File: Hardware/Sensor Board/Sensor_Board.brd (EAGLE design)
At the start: 100 x 80 mm, 3 parts

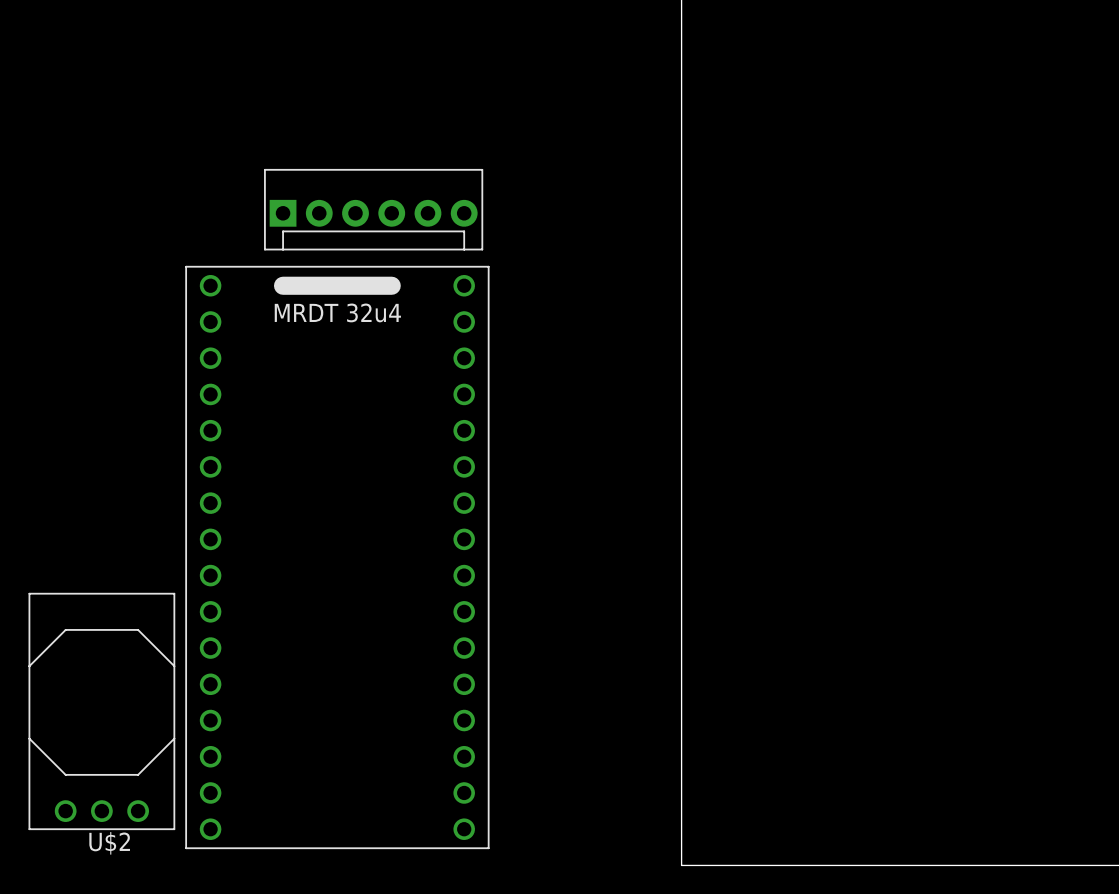
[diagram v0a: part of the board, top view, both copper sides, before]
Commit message: Added most of the components onto the Science board
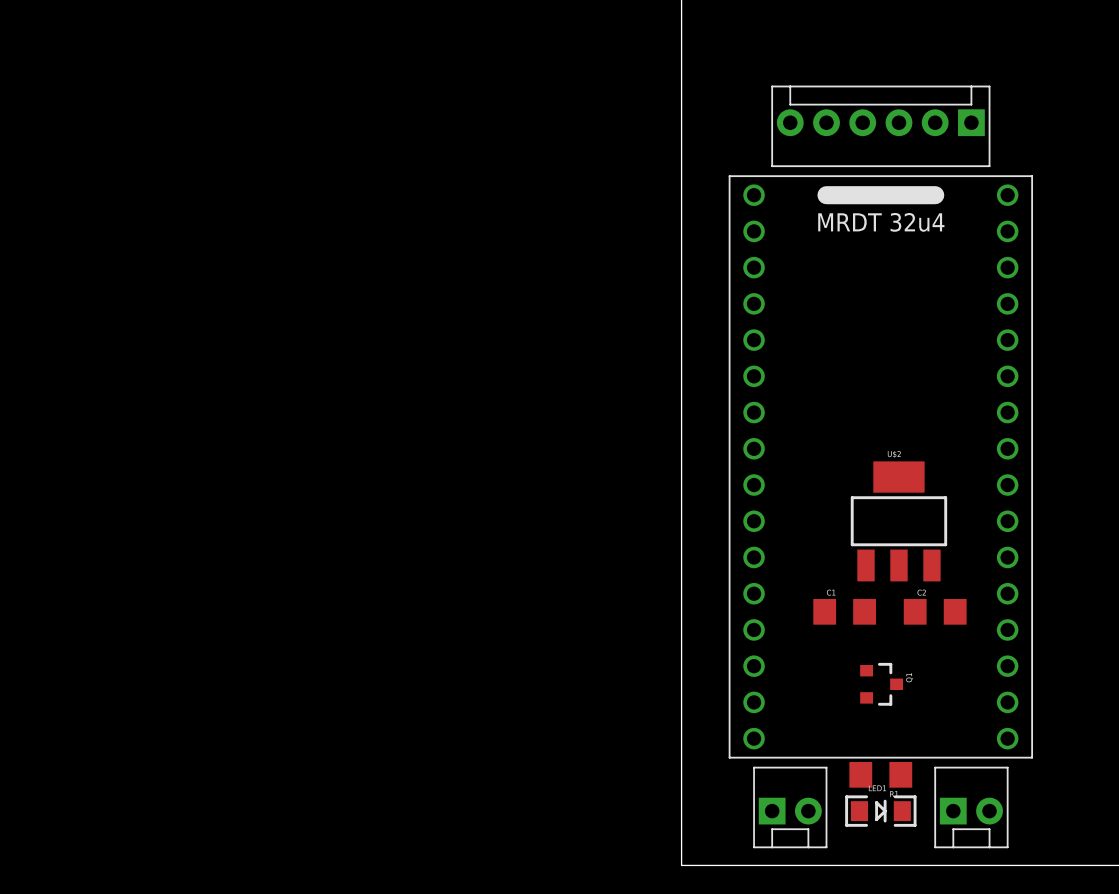
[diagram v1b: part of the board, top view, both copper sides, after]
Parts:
- added C1, C2: .1uF, SparkFun-Passives:1206
- added JP2, JP3: M02POLAR, SparkFun-Connectors:MOLEX-1X2
- added LED1: (no value), SparkFun-LED:LED-1206
- added Q1: MMBT2222A, SparkFun-DiscreteSemi:SOT23-3
- added R1: 1k, SparkFun-Passives:1206
- U$2: value Q_OKI-78SR -> V_REG_LM3940; device MRDT-2015-PowerBoard:OKI-78SRH -> SparkFun-PowerIC:SOT223
- moved U$2 59.5 mm to (15.2, 24.1)
- moved JP1 48.7 mm to (20.3, 52.1), turned to 180 degrees
- moved U$1 38.6 mm to (14.0, 27.9)
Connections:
- removed net N$1: JP1.1
- removed net N$2: JP1.2
- removed net N$3: JP1.3
- removed net N$4: JP1.4
- removed net N$5: JP1.5
- removed net N$6: JP1.6
- new net 3.3V: C2.1, Q1.3, U$1.18, U$2.3
- new net 5V: C1.1, JP1.1, JP2.2, R1.1, U$2.1
- new net GND: C1.2, C2.2, JP1.6, JP2.1, JP3.1, LED1.C, U$1.15, U$1.17, U$2.2
- new net ICG: JP1.2, U$1.32
- new net M: JP1.3, U$1.31
- new net N$11: U$1.28
- new net N$7: JP3.2, Q1.2
- new net N$8: LED1.A, R1.2
- new net OS: JP1.5, U$1.29
- new net SH: JP1.4, U$1.30
- new net TRANS_LASER: Q1.1, U$1.13
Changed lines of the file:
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@@
 </autorouter>
 <elements>
-<element name="U$1" library="MRDT-2015-General" package="32U4_MCU_DIP" value="32U4_BREAKOUT" x="-24.13" y="21.59"/>
-<element name="JP1" library="SparkFun-Connectors" package="MOLEX-1X6" value="" x="-27.94" y="45.72"/>
-<element name="U$2" library="MRDT-2015-PowerBoard" package="OKI-78SRH" value="Q_OKI-78SR" x="-40.64" y="3.81"/>
+<element name="U$1" library="MRDT-2015-General" package="32U4_MCU_DIP" value="32U4_BREAKOUT" x="13.97" y="27.94"/>
+<element name="JP1" library="SparkFun-Connectors" package="MOLEX-1X6" value="" x="20.32" y="52.07" rot="R180"/>
+<element name="JP2" library="SparkFun-Connectors" package="MOLEX-1X2" value="M02POLAR" x="19.05" y="3.81"/>
+<element name="JP3" library="SparkFun-Connectors" package="MOLEX-1X2" value="M02POLAR" x="6.35" y="3.81"/>
+<element name="Q1" library="SparkFun-DiscreteSemi" package="SOT23-3" value="MMBT2222A" x="13.97" y="12.7" rot="R270">
+<attribute name="PROD_ID" value="TRANS-08049" x="13.97" y="12.7" size="1.778" layer="27" rot="R270" display="off"/>
+</element>
+<element name="U$2" library="SparkFun-PowerIC" package="SOT223" value="V_REG_LM3940" x="15.24" y="24.13"/>
+<element name="C1" library="SparkFun-Passives" package="1206" value=".1uF" x="11.43" y="17.78"/>
+<element name="C2" library="SparkFun-Passives" package="1206" value=".1uF" x="17.78" y="17.78"/>
+<element name="LED1" library="SparkFun-LED" package="LED-1206" value="" x="13.97" y="3.81"/>
+<element name="R1" library="SparkFun-Passives" package="1206" value="1k" x="13.97" y="6.35" rot="R180"/>
 </elements>
 <signals>
-<signal name="N$1">
+<signal name="ICG">
+<contactref element="JP1" pad="2"/>
+<contactref element="U$1" pad="32"/>
+<wire x1="17.78" y1="52.07" x2="22.86" y2="46.99" width="0" layer="19" extent="1-1"/>
+</signal>
+<signal name="M">
+<contactref element="JP1" pad="3"/>
+<contactref element="U$1" pad="31"/>
+<wire x1="22.86" y1="44.45" x2="15.24" y2="52.07" width="0" layer="19" extent="1-1"/>
+</signal>
+<signal name="SH">
+<contactref element="JP1" pad="4"/>
+<contactref element="U$1" pad="30"/>
+<wire x1="22.86" y1="41.91" x2="12.7" y2="52.07" width="0" layer="19" extent="1-1"/>
+</signal>
+<signal name="OS">
+<contactref element="JP1" pad="5"/>
+<contactref element="U$1" pad="29"/>
+<wire x1="22.86" y1="39.37" x2="10.16" y2="52.07" width="0" layer="19" extent="1-1"/>
+</signal>
+<signal name="GND">
+<contactref element="JP2" pad="1"/>
+<contactref element="U$1" pad="15"/>
+<contactref element="U$1" pad="17"/>
+<contactref element="JP3" pad="1"/>
+<contactref element="C1" pad="2"/>
+<contactref element="U$2" pad="2"/>
+<contactref element="C2" pad="2"/>
+<contactref element="LED1" pad="C"/>
+<contactref element="JP1" pad="6"/>
+<wire x1="19.18" y1="17.78" x2="15.47" y2="3.81" width="0" layer="19" extent="1-1"/>
+<wire x1="12.83" y1="17.78" x2="19.18" y2="17.78" width="0" layer="19" extent="1-1"/>
+<wire x1="15.24" y1="21.0312" x2="12.83" y2="17.78" width="0" layer="19" extent="1-1"/>
+<wire x1="6.35" y1="3.81" x2="12.83" y2="17.78" width="0" layer="19" extent="1-1"/>
+<wire x1="19.05" y1="3.81" x2="6.35" y2="3.81" width="0" layer="19" extent="1-1"/>
+<wire x1="5.08" y1="11.43" x2="19.05" y2="3.81" width="0" layer="19" extent="1-1"/>
+<wire x1="22.86" y1="8.89" x2="5.08" y2="11.43" width="0" layer="19" extent="1-1"/>
+<wire x1="7.62" y1="52.07" x2="22.86" y2="8.89" width="0" layer="19" extent="1-1"/>
+</signal>
+<signal name="5V">
+<contactref element="JP2" pad="2"/>
+<contactref element="U$2" pad="1"/>
+<contactref element="C1" pad="1"/>
+<contactref element="R1" pad="1"/>
 <contactref element="JP1" pad="1"/>
+<wire x1="10.03" y1="17.78" x2="15.37" y2="6.35" width="0" layer="19" extent="1-1"/>
+<wire x1="12.9286" y1="21.0312" x2="10.03" y2="17.78" width="0" layer="19" extent="1-1"/>
+<wire x1="21.59" y1="3.81" x2="10.03" y2="17.78" width="0" layer="19" extent="1-1"/>
+<wire x1="20.32" y1="52.07" x2="21.59" y2="3.81" width="0" layer="19" extent="1-1"/>
 </signal>
-<signal name="N$2">
-<contactref element="JP1" pad="2"/>
+<signal name="TRANS_LASER">
+<contactref element="U$1" pad="13"/>
+<contactref element="Q1" pad="1"/>
+<wire x1="5.08" y1="16.51" x2="12.97" y2="13.65" width="0" layer="19" extent="1-1"/>
 </signal>
-<signal name="N$3">
-<contactref element="JP1" pad="3"/>
+<signal name="N$7">
+<contactref element="JP3" pad="2"/>
+<contactref element="Q1" pad="2"/>
+<wire x1="8.89" y1="3.81" x2="12.97" y2="11.75" width="0" layer="19" extent="1-1"/>
 </signal>
-<signal name="N$4">
-<contactref element="JP1" pad="4"/>
+<signal name="3.3V">
+<contactref element="Q1" pad="3"/>
+<contactref element="C2" pad="1"/>
+<contactref element="U$2" pad="3"/>
+<contactref element="U$1" pad="18"/>
+<wire x1="17.5514" y1="21.0312" x2="16.38" y2="17.78" width="0" layer="19" extent="1-1"/>
+<wire x1="15.07" y1="12.7" x2="17.5514" y2="21.0312" width="0" layer="19" extent="1-1"/>
+<wire x1="22.86" y1="11.43" x2="15.07" y2="12.7" width="0" layer="19" extent="1-1"/>
 </signal>
-<signal name="N$5">
-<contactref element="JP1" pad="5"/>
+<signal name="N$8">
+<contactref element="R1" pad="2"/>
+<contactref element="LED1" pad="A"/>
+<wire x1="12.47" y1="3.81" x2="12.57" y2="6.35" width="0" layer="19" extent="1-1"/>
 </signal>
-<signal name="N$6">
-<contactref element="JP1" pad="6"/>
+<signal name="N$11">
+<contactref element="U$1" pad="28"/>
 </signal>
 </signals>

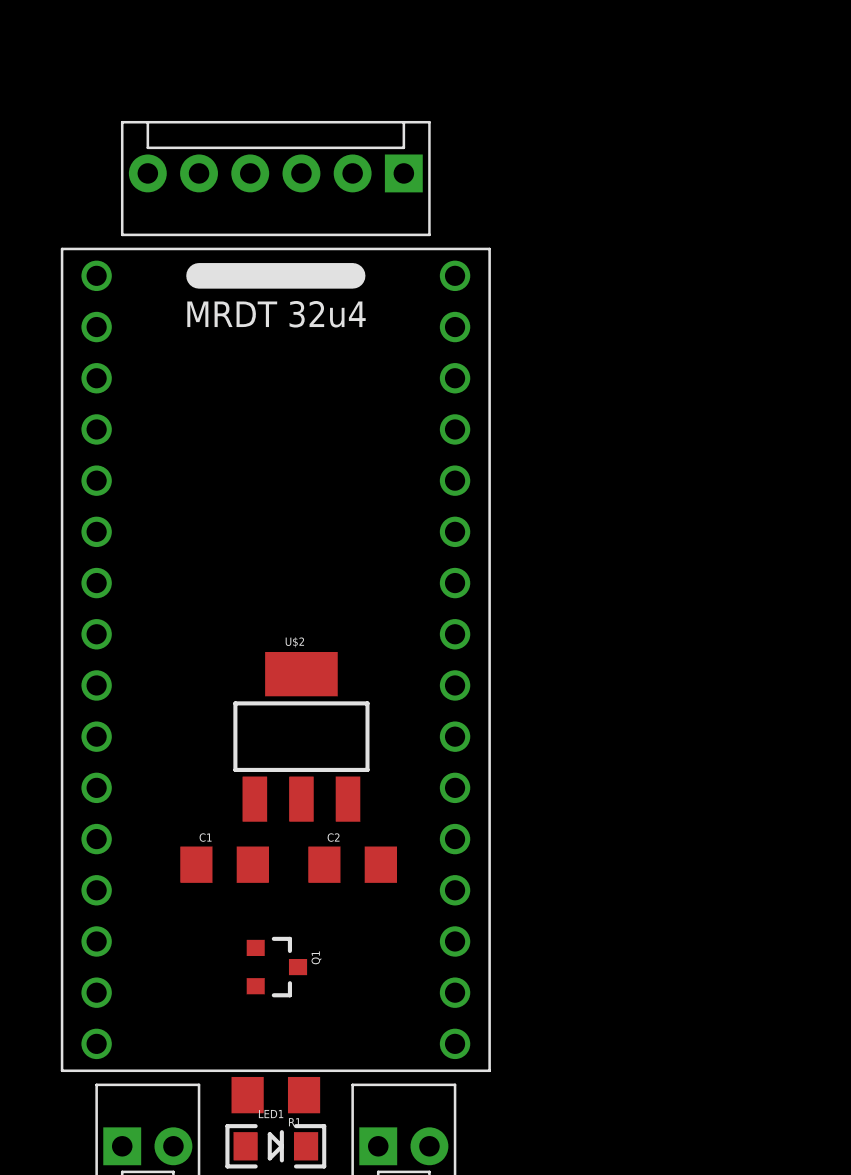
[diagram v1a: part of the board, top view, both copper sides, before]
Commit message: Added 5V power system
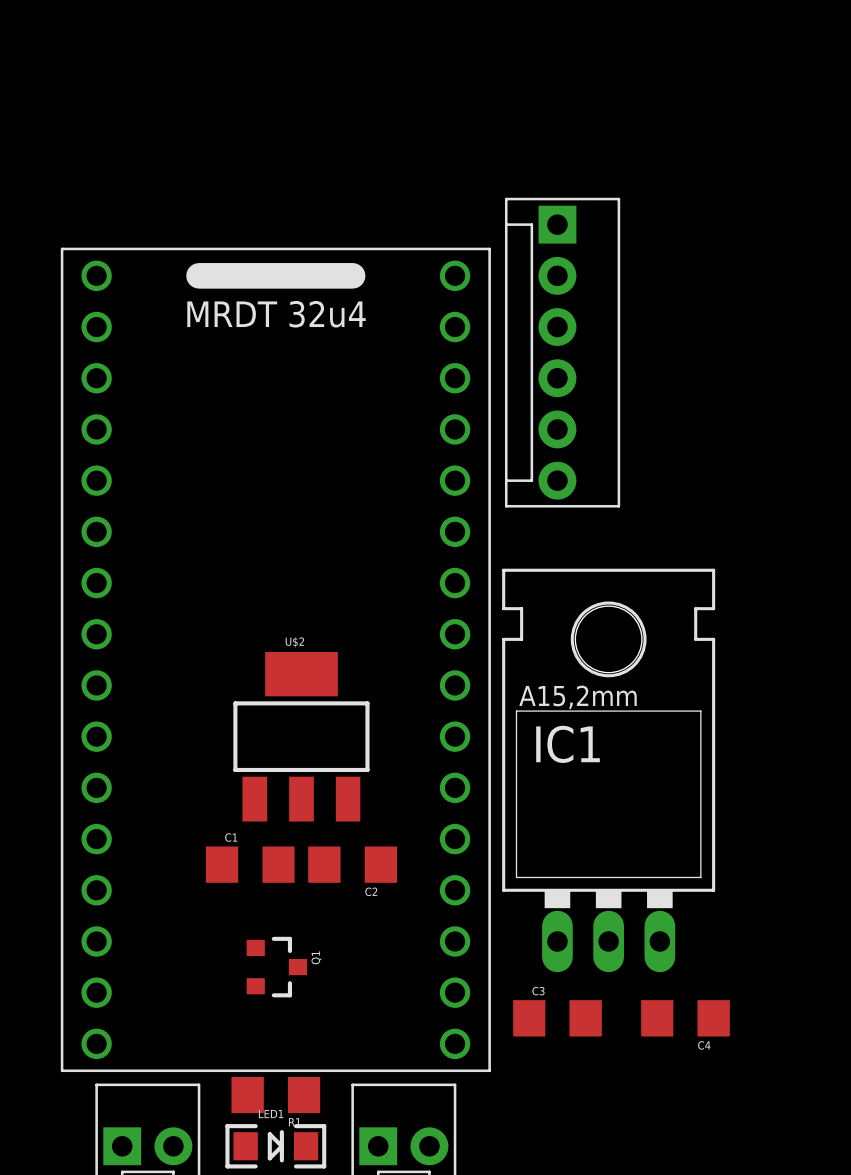
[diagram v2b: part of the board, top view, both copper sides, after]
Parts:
- added C3, C4: .1uF, SparkFun-Passives:1206
- added IC1: (no value), v-reg:78XXL
- moved JP1 8.03 mm to (27.9, 49.5), turned to 270 degrees
- moved C1 1.27 mm to (12.7, 17.8)
- turned C2 to 180 degrees
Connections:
- net 3.3V: now also C3.1, IC1.IN
- net 5V: now also C4.1, IC1.OUT
- net GND: now also C3.2, C4.2, IC1.GND
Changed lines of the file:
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@@
 <?xml version="1.0" encoding="utf-8"?>
 <!DOCTYPE eagle SYSTEM "eagle.dtd">
-<eagle version="6.6.0">
+<eagle version="6.5.0">
 <drawing>
 <settings>
@@
 <layers>
 <layer number="1" name="Top" color="4" fill="1" visible="yes" active="yes"/>
+<layer number="2" name="Route2" color="1" fill="3" visible="no" active="no"/>
+<layer number="3" name="Route3" color="4" fill="3" visible="no" active="no"/>
+<layer number="4" name="Route4" color="1" fill="4" visible="no" active="no"/>
+<layer number="5" name="Route5" color="4" fill="4" visible="no" active="no"/>
+<layer number="6" name="Route6" color="1" fill="8" visible="no" active="no"/>
+<layer number="7" name="Route7" color="4" fill="8" visible="no" active="no"/>
+<layer number="8" name="Route8" color="1" fill="2" visible="no" active="no"/>
+<layer number="9" name="Route9" color="4" fill="2" visible="no" active="no"/>
+<layer number="10" name="Route10" color="1" fill="7" visible="no" active="no"/>
+<layer number="11" name="Route11" color="4" fill="7" visible="no" active="no"/>
+<layer number="12" name="Route12" color="1" fill="5" visible="no" active="no"/>
+<layer number="13" name="Route13" color="4" fill="5" visible="no" active="no"/>
+<layer number="14" name="Route14" color="1" fill="6" visible="no" active="no"/>
+<layer number="15" name="Route15" color="4" fill="6" visible="no" active="no"/>
 <layer number="16" name="Bottom" color="1" fill="1" visible="yes" active="yes"/>
 <layer number="17" name="Pads" color="2" fill="1" visible="yes" active="yes"/>
@@
 <elements>
 <element name="U$1" library="MRDT-2015-General" package="32U4_MCU_DIP" value="32U4_BREAKOUT" x="13.97" y="27.94"/>
-<element name="JP1" library="SparkFun-Connectors" package="MOLEX-1X6" value="" x="20.32" y="52.07" rot="R180"/>
+<element name="JP1" library="SparkFun-Connectors" package="MOLEX-1X6" value="" x="27.94" y="49.53" rot="R270"/>
 <element name="JP2" library="SparkFun-Connectors" package="MOLEX-1X2" value="M02POLAR" x="19.05" y="3.81"/>
 <element name="JP3" library="SparkFun-Connectors" package="MOLEX-1X2" value="M02POLAR" x="6.35" y="3.81"/>
@@
 </element>
 <element name="U$2" library="SparkFun-PowerIC" package="SOT223" value="V_REG_LM3940" x="15.24" y="24.13"/>
-<element name="C1" library="SparkFun-Passives" package="1206" value=".1uF" x="11.43" y="17.78"/>
-<element name="C2" library="SparkFun-Passives" package="1206" value=".1uF" x="17.78" y="17.78"/>
+<element name="C1" library="SparkFun-Passives" package="1206" value=".1uF" x="12.7" y="17.78"/>
+<element name="C2" library="SparkFun-Passives" package="1206" value=".1uF" x="17.78" y="17.78" rot="R180"/>
 <element name="LED1" library="SparkFun-LED" package="LED-1206" value="" x="13.97" y="3.81"/>
 <element name="R1" library="SparkFun-Passives" package="1206" value="1k" x="13.97" y="6.35" rot="R180"/>
+<element name="IC1" library="v-reg" package="78XXL" value="" x="30.48" y="17.78"/>
+<element name="C3" library="SparkFun-Passives" package="1206" value=".1uF" x="27.94" y="10.16"/>
+<element name="C4" library="SparkFun-Passives" package="1206" value=".1uF" x="34.29" y="10.16" rot="R180"/>
 </elements>
 <signals>
@@
 <contactref element="JP1" pad="2"/>
 <contactref element="U$1" pad="32"/>
-<wire x1="17.78" y1="52.07" x2="22.86" y2="46.99" width="0" layer="19" extent="1-1"/>
+<wire x1="27.94" y1="46.99" x2="22.86" y2="46.99" width="0" layer="19" extent="1-1"/>
 </signal>
 <signal name="M">
 <contactref element="JP1" pad="3"/>
 <contactref element="U$1" pad="31"/>
-<wire x1="22.86" y1="44.45" x2="15.24" y2="52.07" width="0" layer="19" extent="1-1"/>
+<wire x1="22.86" y1="44.45" x2="27.94" y2="44.45" width="0" layer="19" extent="1-1"/>
 </signal>
 <signal name="SH">
 <contactref element="JP1" pad="4"/>
 <contactref element="U$1" pad="30"/>
-<wire x1="22.86" y1="41.91" x2="12.7" y2="52.07" width="0" layer="19" extent="1-1"/>
+<wire x1="22.86" y1="41.91" x2="27.94" y2="41.91" width="0" layer="19" extent="1-1"/>
 </signal>
 <signal name="OS">
 <contactref element="JP1" pad="5"/>
 <contactref element="U$1" pad="29"/>
-<wire x1="22.86" y1="39.37" x2="10.16" y2="52.07" width="0" layer="19" extent="1-1"/>
+<wire x1="22.86" y1="39.37" x2="27.94" y2="39.37" width="0" layer="19" extent="1-1"/>
 </signal>
 <signal name="GND">
@@
 <contactref element="LED1" pad="C"/>
 <contactref element="JP1" pad="6"/>
-<wire x1="19.18" y1="17.78" x2="15.47" y2="3.81" width="0" layer="19" extent="1-1"/>
-<wire x1="12.83" y1="17.78" x2="19.18" y2="17.78" width="0" layer="19" extent="1-1"/>
-<wire x1="15.24" y1="21.0312" x2="12.83" y2="17.78" width="0" layer="19" extent="1-1"/>
-<wire x1="6.35" y1="3.81" x2="12.83" y2="17.78" width="0" layer="19" extent="1-1"/>
-<wire x1="19.05" y1="3.81" x2="6.35" y2="3.81" width="0" layer="19" extent="1-1"/>
-<wire x1="5.08" y1="11.43" x2="19.05" y2="3.81" width="0" layer="19" extent="1-1"/>
-<wire x1="22.86" y1="8.89" x2="5.08" y2="11.43" width="0" layer="19" extent="1-1"/>
-<wire x1="7.62" y1="52.07" x2="22.86" y2="8.89" width="0" layer="19" extent="1-1"/>
+<contactref element="C4" pad="2"/>
+<contactref element="C3" pad="2"/>
+<contactref element="IC1" pad="GND"/>
+<wire x1="15.24" y1="21.0312" x2="27.94" y2="36.83" width="0" layer="19" extent="1-1"/>
+<wire x1="14.1" y1="17.78" x2="15.24" y2="21.0312" width="0" layer="19" extent="1-1"/>
+<wire x1="16.38" y1="17.78" x2="15.24" y2="21.0312" width="0" layer="19" extent="1-1"/>
+<wire x1="22.86" y1="8.89" x2="16.38" y2="17.78" width="0" layer="19" extent="1-1"/>
+<wire x1="19.05" y1="3.81" x2="22.86" y2="8.89" width="0" layer="19" extent="1-1"/>
+<wire x1="15.47" y1="3.81" x2="19.05" y2="3.81" width="0" layer="19" extent="1-1"/>
+<wire x1="6.35" y1="3.81" x2="15.47" y2="3.81" width="0" layer="19" extent="1-1"/>
+<wire x1="5.08" y1="11.43" x2="6.35" y2="3.81" width="0" layer="19" extent="1-1"/>
+<wire x1="30.48" y1="13.97" x2="6.35" y2="3.81" width="0" layer="19" extent="1-1"/>
+<wire x1="29.34" y1="10.16" x2="30.48" y2="13.97" width="0" layer="19" extent="1-1"/>
+<wire x1="32.89" y1="10.16" x2="29.34" y2="10.16" width="0" layer="19" extent="1-1"/>
 </signal>
 <signal name="5V">
@@
 <contactref element="R1" pad="1"/>
 <contactref element="JP1" pad="1"/>
-<wire x1="10.03" y1="17.78" x2="15.37" y2="6.35" width="0" layer="19" extent="1-1"/>
-<wire x1="12.9286" y1="21.0312" x2="10.03" y2="17.78" width="0" layer="19" extent="1-1"/>
-<wire x1="21.59" y1="3.81" x2="10.03" y2="17.78" width="0" layer="19" extent="1-1"/>
-<wire x1="20.32" y1="52.07" x2="21.59" y2="3.81" width="0" layer="19" extent="1-1"/>
+<contactref element="IC1" pad="OUT"/>
+<contactref element="C4" pad="1"/>
+<wire x1="12.9286" y1="21.0312" x2="27.94" y2="49.53" width="0" layer="19" extent="1-1"/>
+<wire x1="11.3" y1="17.78" x2="12.9286" y2="21.0312" width="0" layer="19" extent="1-1"/>
+<wire x1="15.37" y1="6.35" x2="11.3" y2="17.78" width="0" layer="19" extent="1-1"/>
+<wire x1="21.59" y1="3.81" x2="15.37" y2="6.35" width="0" layer="19" extent="1-1"/>
+<wire x1="33.02" y1="13.97" x2="15.37" y2="6.35" width="0" layer="19" extent="1-1"/>
+<wire x1="35.69" y1="10.16" x2="33.02" y2="13.97" width="0" layer="19" extent="1-1"/>
 </signal>
 <signal name="TRANS_LASER">
@@
 <contactref element="U$2" pad="3"/>
 <contactref element="U$1" pad="18"/>
-<wire x1="17.5514" y1="21.0312" x2="16.38" y2="17.78" width="0" layer="19" extent="1-1"/>
-<wire x1="15.07" y1="12.7" x2="17.5514" y2="21.0312" width="0" layer="19" extent="1-1"/>
+<contactref element="C3" pad="1"/>
+<contactref element="IC1" pad="IN"/>
+<wire x1="19.18" y1="17.78" x2="17.5514" y2="21.0312" width="0" layer="19" extent="1-1"/>
+<wire x1="15.07" y1="12.7" x2="19.18" y2="17.78" width="0" layer="19" extent="1-1"/>
 <wire x1="22.86" y1="11.43" x2="15.07" y2="12.7" width="0" layer="19" extent="1-1"/>
+<wire x1="27.94" y1="13.97" x2="15.07" y2="12.7" width="0" layer="19" extent="1-1"/>
+<wire x1="26.54" y1="10.16" x2="27.94" y2="13.97" width="0" layer="19" extent="1-1"/>
 </signal>
 <signal name="N$8">
